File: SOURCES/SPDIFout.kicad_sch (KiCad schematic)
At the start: 24 parts, among them J3 RCA_01, J4 RCA_01, P11 FCR684205T, P12 FCR684205R, P19 TST, P27 TST, T1 Transformer_1P_1S_DA101JC, T2 Transformer_1P_1S_DA101JC, U6 CS8406-CZZ

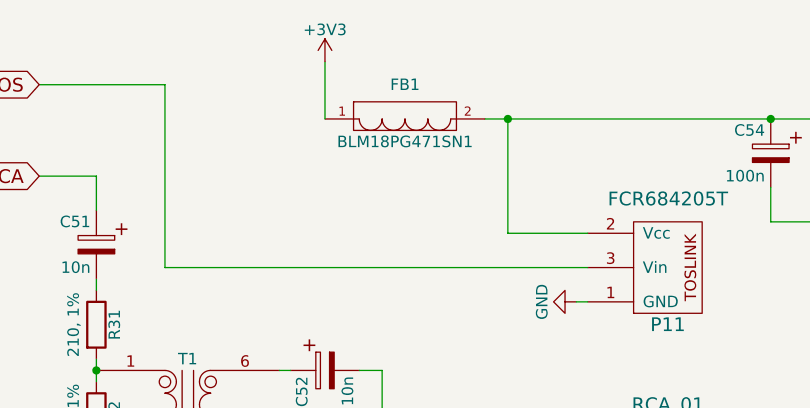
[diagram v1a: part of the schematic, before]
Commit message: Removed redundant 7414 and pot, rerouted a bit.
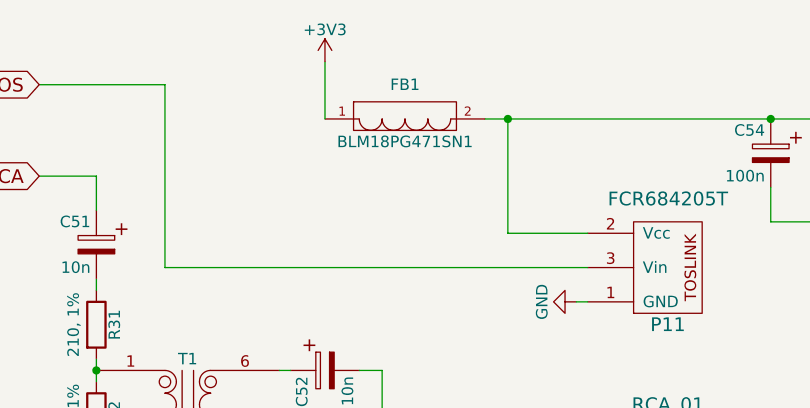
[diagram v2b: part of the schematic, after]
